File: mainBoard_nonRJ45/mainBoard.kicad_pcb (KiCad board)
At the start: 4 copper layers, 110 x 75 mm, 79 parts, among them IC1 TCAN3414DR, J1 XT60PW-M, J10 XT30U-M, J11 XT30U-M, J12 Conn_01x03, J13 BM02B-SRSS-TB, J14 BM02B-SRSS-TB, J15 BM02B-SRSS-TB, J16 BM04B-SRSS-TB, J17 BM04B-SRSS-TB, J18 BM04B-SRSS-TB, J19 BM04B-SRSS-TB, J2 XT60PW-M, J20 BM04B-SRSS-TB, J21 B2B-PH_K, J22 Conn_01x02, J23 Conn_02x04_Odd_Even, J24 BM02B-SRSS-TB, J25 BM02B-SRSS-TB, J3 XT30PW-M, J4 XT30PW-M, J5 Barrel_Jack, J6 XT30U_M, J7 XT30U-M, J8 XT30U-M, J9 XT30U-M, Q1 FQD11P06TM, Q2 FQD11P06TM, U1 TPS565208, U2 TPS565208, U3 TCA9548APWR

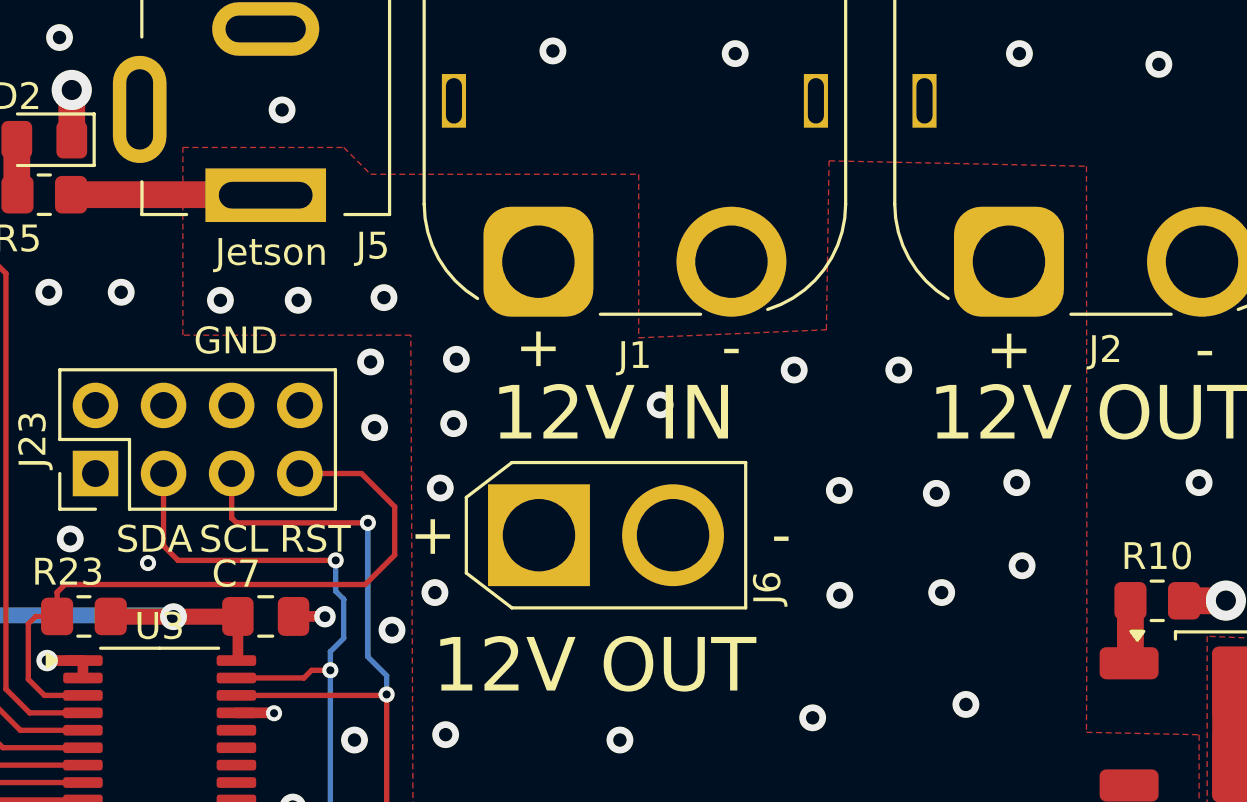
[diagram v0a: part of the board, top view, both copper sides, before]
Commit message: Fixed trace that had a unecessary via
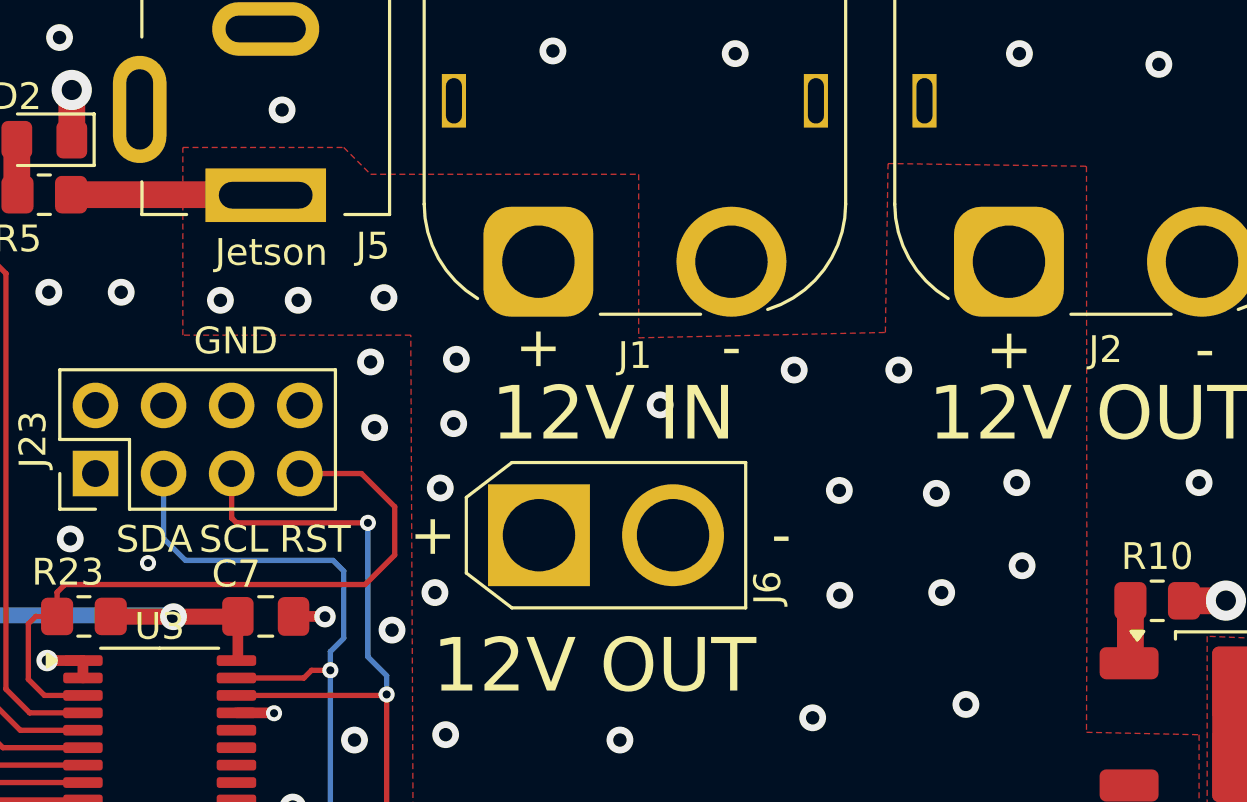
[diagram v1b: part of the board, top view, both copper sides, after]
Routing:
- net SDA1: track 54.6 -> 54.4 mm, vias 3 -> 2
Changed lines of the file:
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@@
-	)
-	(segment
-		(start 39.265 47.172643)
-		(end 39.265 44.475)
-		(width 0.2)
-		(layer "F.Cu")
-		(net 22)
 	)
 	(segment
@@
 	)
 	(segment
-		(start 45.685786 47.714215)
-		(end 39.806572 47.714215)
-		(width 0.2)
-		(layer "F.Cu")
-		(net 22)
-	)
-	(segment
 		(start 44.785786 51.814215)
 		(end 44.500001 52.1)
-		(width 0.2)
-		(layer "F.Cu")
-		(net 22)
-	)
-	(segment
-		(start 39.806572 47.714215)
-		(end 39.265 47.172643)
 		(width 0.2)
 		(layer "F.Cu")
@@
 		(net 22)
 	)
-	(via
-		(at 45.685786 47.714215)
-		(size 0.6)
-		(drill 0.3)
-		(layers "F.Cu" "B.Cu")
+	(segment
+		(start 45.985786 50.614215)
+		(end 45.985786 48.114215)
+		(width 0.2)
+		(layer "B.Cu")
+		(net 22)
+	)
+	(segment
+		(start 45.585786 47.714215)
+		(end 40.085786 47.714215)
+		(width 0.2)
+		(layer "B.Cu")
+		(net 22)
+	)
+	(segment
+		(start 45.985786 48.114215)
+		(end 45.585786 47.714215)
+		(width 0.2)
+		(layer "B.Cu")
+		(net 22)
+	)
+	(segment
+		(start 39.265 46.893429)
+		(end 39.265 44.475)
+		(width 0.2)
+		(layer "B.Cu")
+		(net 22)
+	)
+	(segment
+		(start 40.085786 47.714215)
+		(end 39.265 46.893429)
+		(width 0.2)
+		(layer "B.Cu")
+		(net 22)
+	)
+	(segment
+		(start 23.385786 66.814215)
+		(end 23.385786 68.814215)
+		(width 0.2)
+		(layer "B.Cu")
 		(net 22)
 	)
@@
 	)
 	(segment
-		(start 45.685786 48.864215)
-		(end 45.685786 47.714215)
-		(width 0.2)
-		(layer "B.Cu")
-		(net 22)
-	)
-	(segment
-		(start 23.385786 66.814215)
-		(end 23.385786 68.814215)
-		(width 0.2)
-		(layer "B.Cu")
-		(net 22)
-	)
-	(segment
 		(start 45.485786 51.814215)
 		(end 45.485786 51.114215)
@@
 		(start 45.485786 59.514215)
 		(end 42.585786 62.414215)
-		(width 0.2)
-		(layer "B.Cu")
-		(net 22)
-	)
-	(segment
-		(start 45.985786 50.614215)
-		(end 45.985786 49.164215)
-		(width 0.2)
-		(layer "B.Cu")
-		(net 22)
-	)
-	(segment
-		(start 45.985786 49.164215)
-		(end 45.685786 48.864215)
 		(width 0.2)
 		(layer "B.Cu")
@@
 			(pts
 				(xy 39.985786 32.314215) (xy 45.985786 32.314215) (xy 46.985786 33.314215) (xy 56.985786 33.314215)
-				(xy 56.985786 39.414215) (xy 63.985786 39.114215) (xy 64.085786 32.814215) (xy 73.685786 33.014215)
+				(xy 56.985786 39.414215) (xy 66.185786 39.214215) (xy 66.285786 32.914215) (xy 73.685786 33.014215)
 				(xy 73.701321 50.22975) (xy 73.685786 54.12579) (xy 77.885786 54.216896) (xy 77.885786 62.414215)
 				(xy 80.682821 62.311175) (xy 88.468804 62.314215) (xy 104.24746 62.814215) (xy 108.786664 62.814215)

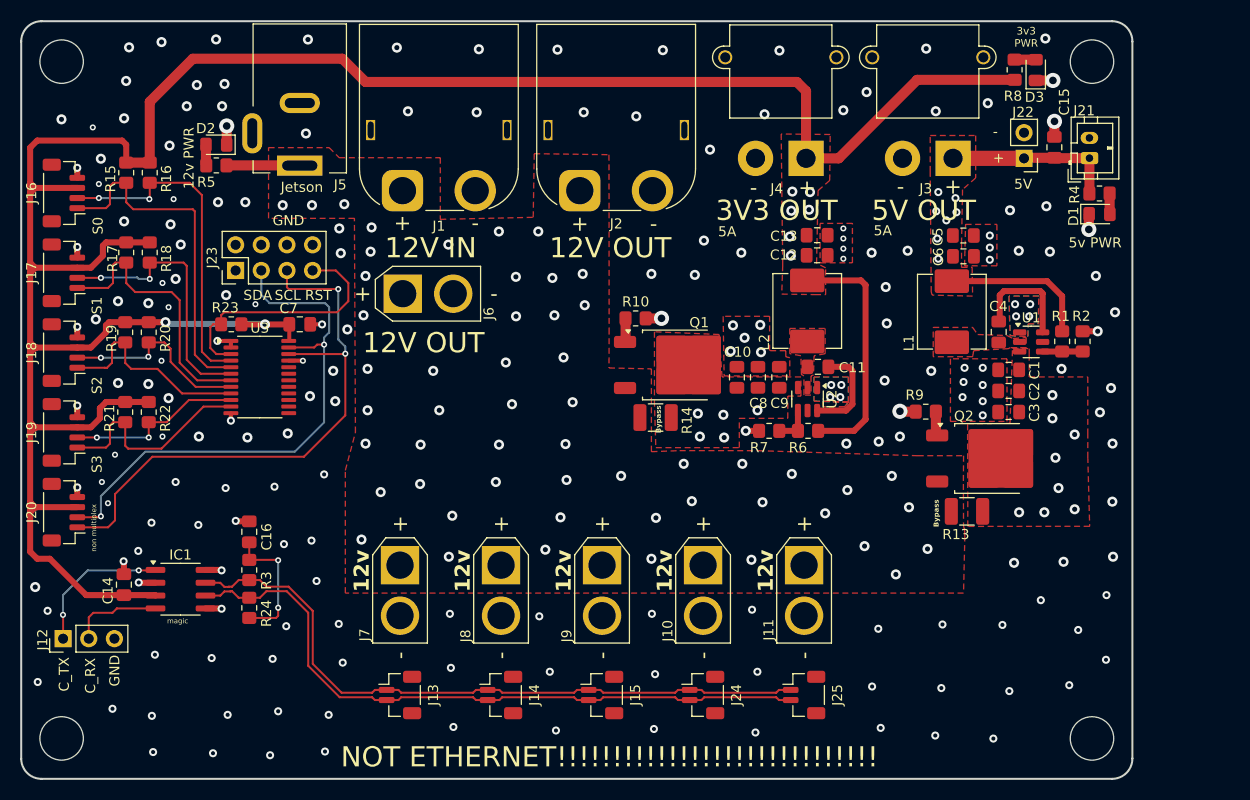
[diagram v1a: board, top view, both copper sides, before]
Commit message: move extra XT30 to bottom
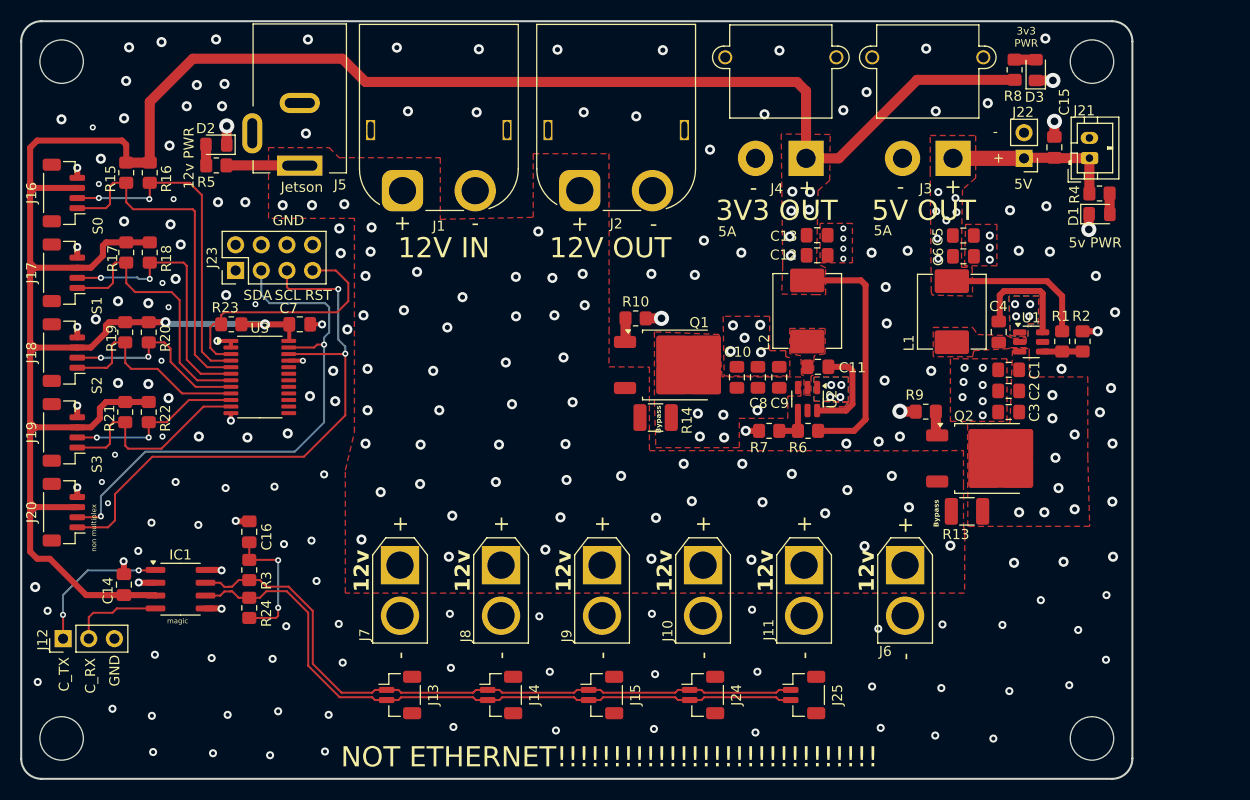
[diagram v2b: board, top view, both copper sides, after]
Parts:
- moved J6 56.5 mm to (103.0, 73.7), turned to -90 degrees
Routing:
- net +12V: vias 53 -> 54
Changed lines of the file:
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@@
 	(footprint "Connector_AMASS:AMASS_XT30U-M_1x02_P5.0mm_Vertical"
 		(layer "F.Cu")
-		(at 53.266571 46.775001)
+		(at 103 73.65 -90)
 		(descr "Connector XT30 Vertical Cable Male, https://www.tme.eu/en/Document/3cbfa5cfa544d79584972dd5234a409e/XT30U%20SPEC.pdf")
 		(tags "RC Connector XT30")
 		(property "Reference" "J6"
-			(at 8.530001 1.958429 90)
+			(at 8.530001 1.958429 0)
 			(layer "F.SilkS")
 			(effects
@@
 		)
 		(property "Value" "XT30U_M"
-			(at 2.5 4 0)
+			(at 2.5 4 90)
 			(layer "F.Fab")
 			(hide yes)
@@
 		)
 		(property "Footprint" "Connector_AMASS:AMASS_XT30U-M_1x02_P5.0mm_Vertical"
-			(at 0 0 0)
+			(at 0 0 -90)
 			(unlocked yes)
 			(layer "F.Fab")
@@
 		)
 		(property "Datasheet" ""
-			(at 0 0 0)
+			(at 0 0 -90)
 			(unlocked yes)
 			(layer "F.Fab")
@@
 		)
 		(property "Description" "Generic connector, single row, 01x02, script generated (kicad-library-utils/schlib/autogen/connector/)"
-			(at 0 0 0)
+			(at 0 0 -90)
 			(unlocked yes)
 			(layer "F.Fab")
@@
 		(attr through_hole)
 		(fp_line
-			(start -2.71 -1.41)
-			(end -2.71 1.41)
+			(start -1.01 2.71)
+			(end 7.71 2.71)
 			(stroke
 				(width 0.12)
@@
 		)
 		(fp_line
-			(start -2.71 -1.41)
-			(end -1.01 -2.71)
+			(start -2.71 1.41)
+			(end -1.01 2.71)
 			(stroke
 				(width 0.12)
@@
 		)
 		(fp_line
-			(start -2.71 1.41)
-			(end -1.01 2.71)
+			(start -2.71 -1.41)
+			(end -2.71 1.41)
 			(stroke
 				(width 0.12)
@@
 		)
 		(fp_line
-			(start -1.01 -2.71)
-			(end 7.71 -2.71)
+			(start -2.71 -1.41)
+			(end -1.01 -2.71)
 			(stroke
 				(width 0.12)
@@
 		)
 		(fp_line
-			(start -1.01 2.71)
-			(end 7.71 2.71)
+			(start -1.01 -2.71)
+			(end 7.71 -2.71)
 			(stroke
 				(width 0.12)
@@
 		)
 		(fp_line
-			(start -3.1 -1.8)
-			(end -3.1 1.8)
+			(start -1.4 3.1)
+			(end 8.1 3.1)
 			(stroke
 				(width 0.05)
@@
 		)
 		(fp_line
-			(start -3.1 -1.8)
-			(end -1.4 -3.1)
+			(start -3.1 1.8)
+			(end -1.4 3.1)
 			(stroke
 				(width 0.05)
@@
 		)
 		(fp_line
-			(start -3.1 1.8)
-			(end -1.4 3.1)
+			(start -3.1 -1.8)
+			(end -3.1 1.8)
 			(stroke
 				(width 0.05)
@@
 		)
 		(fp_line
-			(start -1.4 -3.1)
-			(end 8.1 -3.1)
+			(start -3.1 -1.8)
+			(end -1.4 -3.1)
 			(stroke
 				(width 0.05)
@@
 		)
 		(fp_line
-			(start -1.4 3.1)
-			(end 8.1 3.1)
+			(start -1.4 -3.1)
+			(end 8.1 -3.1)
 			(stroke
 				(width 0.05)
@@
 		)
 		(fp_line
-			(start -2.6 -1.3)
-			(end -2.6 1.3)
+			(start -0.9 2.6)
+			(end 7.6 2.6)
 			(stroke
 				(width 0.1)
@@
 		)
 		(fp_line
-			(start -2.6 -1.3)
-			(end -0.9 -2.6)
+			(start -2.6 1.3)
+			(end -0.9 2.6)
 			(stroke
 				(width 0.1)
@@
 		)
 		(fp_line
-			(start -2.6 1.3)
-			(end -0.9 2.6)
+			(start -2.6 -1.3)
+			(end -2.6 1.3)
 			(stroke
 				(width 0.1)
@@
 		)
 		(fp_line
-			(start -0.9 -2.6)
-			(end 7.6 -2.6)
+			(start -2.6 -1.3)
+			(end -0.9 -2.6)
 			(stroke
 				(width 0.1)
@@
 		)
 		(fp_line
-			(start -0.9 2.6)
-			(end 7.6 2.6)
+			(start -0.9 -2.6)
+			(end 7.6 -2.6)
 			(stroke
 				(width 0.1)
@@
 		)
 		(fp_text user "-"
-			(at 9.03843 0 0)
+			(at 9.03843 0 90)
 			(layer "F.SilkS")
 			(effects
@@
 		)
 		(fp_text user "+"
-			(at -3.96157 0 0)
+			(at -3.96157 0 90)
 			(layer "F.SilkS")
 			(effects
@@
 		)
 		(fp_text user "${REFERENCE}"
-			(at 2.5 0 0)
+			(at 2.5 0 90)
 			(layer "F.Fab")
 			(effects
@@
 		)
 		(pad "1" thru_hole rect
-			(at 0 0)
+			(at 0 0 270)
 			(size 3.8 3.8)
 			(drill 2.7)
@@
 		)
 		(pad "2" thru_hole circle
-			(at 5 0)
+			(at 5 0 270)
 			(size 3.8 3.8)
 			(drill 2.7)
@@
 		)
 	)
+	(gr_text "12v"
+		(at 100.085786 76.314215 90)
+		(layer "F.SilkS")
+		(effects
+			(font
+				(size 1.5 1.5)
+				(thickness 0.3)
+				(bold yes)
+			)
+			(justify left bottom)
+		)
+	)
 	(gr_text "S1"
 		(at 23.585786 48.814215 90)
@@
 		)
 	)
-	(gr_text "12V OUT"
-		(at 49.285786 52.814215 0)
-		(layer "F.SilkS")
-		(effects
-			(font
-				(size 2 2)
-				(thickness 0.25)
-			)
-			(justify left bottom)
-		)
-	)
 	(gr_text "-"
 		(at 111.685786 31.314215 0)
@@
 		)
 	)
-	(gr_text "12V IN"
-		(at 51.485786 43.414215 0)
-		(layer "F.SilkS")
-		(effects
-			(font
-				(size 2 2)
-				(thickness 0.25)
-			)
-			(justify left bottom)
-		)
-	)
 	(gr_text "5V OUT"
 		(at 99.685786 39.714215 0)
@@
 		)
 	)
+	(gr_text "12V IN\n"
+		(at 52.785786 43.414215 0)
+		(layer "F.SilkS")
+		(effects
+			(font
+				(size 2 2)
+				(thickness 0.25)
+			)
+			(justify left bottom)
+		)
+	)
 	(gr_text "Jetson "
 		(at 43.285786 36.814215 0)
@@
 	)
 	(via
-		(at 105.218761 72.040518)
+		(at 107.485786 71.714215)
 		(size 1)
 		(drill 0.5)
@@
 	)
 	(via
-		(at 71.285786 47.914215)
+		(at 59.185786 47.114215)
 		(size 1)
 		(drill 0.5)
@@
 	)
 	(via
-		(at 86.885786 63.614215)
+		(at 71.285786 47.914215)
 		(size 1)
 		(drill 0.5)
@@
 	)
 	(via
-		(at 95.085786 68.514215)
+		(at 86.885786 63.614215)
 		(size 1)
 		(drill 0.5)
@@
 	)
 	(via
-		(at 68.085786 45.214215)
+		(at 95.085786 68.514215)
 		(size 1)
 		(drill 0.5)
@@
 	)
 	(via
-		(at 69.381959 61.661065)
+		(at 68.085786 45.214215)
 		(size 1)
 		(drill 0.5)
@@
 	)
 	(via
-		(at 102.085786 74.564215)
+		(at 69.381959 61.661065)
 		(size 1)
 		(drill 0.5)
@@
 	)
 	(via
-		(at 57.785786 41.914215)
+		(at 54.685786 44.614215)
 		(size 1)
 		(drill 0.5)
@@
 	)
 	(via
-		(at 62.785786 40.614215)
+		(at 57.685786 50.114215)
+		(size 1)
+		(drill 0.5)
+		(layers "F.Cu" "B.Cu")
+		(free yes)
+		(net 15)
+	)
+	(via
+		(at 53.385786 48.414215)
 		(size 1)
 		(drill 0.5)
@@
 		(polygon
 			(pts
-				(xy 39.985786 32.314215) (xy 45.985786 32.314215) (xy 46.985786 33.314215) (xy 56.985786 33.314215)
-				(xy 56.985786 39.414215) (xy 66.185786 39.214215) (xy 66.285786 32.914215) (xy 73.685786 33.014215)
-				(xy 73.701321 50.22975) (xy 73.685786 54.12579) (xy 77.885786 54.216896) (xy 77.885786 62.414215)
-				(xy 80.682821 62.311175) (xy 88.468804 62.314215) (xy 104.24746 62.814215) (xy 108.786664 62.814215)
-				(xy 108.768679 65.614215) (xy 108.785786 69.754755) (xy 108.885786 70.214215) (xy 108.914162 70.714215)
-				(xy 108.785786 76.414215) (xy 47.585786 76.414215) (xy 47.585786 64.264215) (xy 48.585786 60.514215)
-				(xy 48.485786 39.314215) (xy 39.985786 39.314215)
+				(xy 39.984908 32.314215) (xy 45.984908 32.314215) (xy 46.984908 33.314215) (xy 56.984908 33.314215)
+				(xy 56.984908 39.414215) (xy 66.184908 39.214215) (xy 66.184908 32.914215) (xy 73.684908 32.914215)
+				(xy 73.700443 50.22975) (xy 73.684908 54.014215) (xy 77.684908 54.041008) (xy 77.684908 62.314215)
+				(xy 80.681943 62.311175) (xy 88.467926 62.314215) (xy 103.785786 62.325951) (xy 108.773089 62.301518)
+				(xy 108.785786 65.614215) (xy 108.785786 69.806864) (xy 108.884908 70.214215) (xy 108.913284 70.714215)
+				(xy 108.885786 76.414215) (xy 47.584908 76.414215) (xy 47.584908 64.264215) (xy 48.484908 60.514215)
+				(xy 48.484908 39.314215) (xy 39.984908 39.314215)
 			)
 		)
@@
 	(group ""
 		(members "55eb926d-c48c-472f-a188-d87168ec9e24" "5cea113e-1f0e-4d9a-9085-85ed1237b3a7"
-			"ccc775ed-b58e-4e8e-b547-0338de09f7e3" "d860957f-c20a-46b6-814b-eba01f831137"
-			"e5d26f40-7179-4929-b4d4-7448912c413f"
+			"860da3fb-7086-4fa1-a589-ebf19ad6aa41" "ccc775ed-b58e-4e8e-b547-0338de09f7e3"
+			"d860957f-c20a-46b6-814b-eba01f831137" "e5d26f40-7179-4929-b4d4-7448912c413f"
 		)
 	)

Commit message: Reviewed PCB with justin and made changes
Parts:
- added G***: LOGO, LOGO, F.Cu at (61.6, 58.3)
- added J26: BM02B-SRSS-TB, Connector_JST:JST_SH_BM02B-SRSS-TB_1x02-1MP_P1.00mm_Vertical, F.Cu at (103.0, 86.5)
- added R11: 10K, Resistor_SMD:R_0805_2012Metric_Pad1.20x1.40mm_HandSolder, F.Cu at (93.3, 63.3)
- added R12: 10K, Resistor_SMD:R_0805_2012Metric_Pad1.20x1.40mm_HandSolder, F.Cu at (122.8, 52.4)
- added R25: 4.7K, Resistor_SMD:R_0805_2012Metric_Pad1.20x1.40mm_HandSolder, F.Cu at (28.1, 65.8)
- added R26: 4.7K, Resistor_SMD:R_0805_2012Metric_Pad1.20x1.40mm_HandSolder, F.Cu at (25.8, 65.8)
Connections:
- U1 pad 5: unconnected-(U1-EN-Pad5) -> Net-(U1-EN)
- U2 pad 5: unconnected-(U2-EN-Pad5) -> Net-(U2-EN)
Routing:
- net +12V: track 7.24 -> 39.6 mm, vias 54 -> 55
- net CANN: track 67.1 -> 77.3 mm
- net CANP: track 67.1 -> 77.3 mm
- net SCL1: track 57.9 -> 67.3 mm
- net +3V3: track 272.2 -> 281.5 mm
- net Net-(U1-EN): track 0.00 -> 6.23 mm
- net SDA1: track 54.4 -> 58.4 mm
- net Net-(U2-EN): track 0.00 -> 3.99 mm
- net GND: track 30.6 -> 30.5 mm, vias 194 -> 189
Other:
- board text added: "100% NOT ETHERNET!!!!!!!!!!!!!!!!!!!!!!!!!!!!!"
- board text added: "JC (yetanotheryay)"
- board text removed: "NOT ETHERNET!!!!!!!!!!!!!!!!!!!!!!!!!!!!!"
